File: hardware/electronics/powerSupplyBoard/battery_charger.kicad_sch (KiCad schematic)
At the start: 35 parts, among them J5 VAL, J6 VAL, Q1 BUK961R6, U1 BQ25798

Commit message: renamed bms board to power supply board
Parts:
- D1: footprint (none) -> DS-LED-SMD:LTST-1206
- F1: footprint (none) -> DS-Fuses:PTS1206
- L1: footprint (none) -> DS-Inductors-SMD:HCM1A1105V2
- Q1: footprint (none) -> DS-Package-SO:SOT404
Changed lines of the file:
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@@
 		)
 		(instances
-			(project "bms_breakout"
+			(project "powerSupplyBoard"
 				(path "/6f3ae1d2-e925-4178-b812-ea14ec542b6c/391a8be7-2326-4149-9988-5c06224e0655"
 					(reference "C4")
@@
 		)
 		(instances
-			(project "bms_breakout"
+			(project "powerSupplyBoard"
 				(path "/6f3ae1d2-e925-4178-b812-ea14ec542b6c/391a8be7-2326-4149-9988-5c06224e0655"
 					(reference "#PWR016")
@@
 		)
 		(instances
-			(project "bms_breakout"
+			(project "powerSupplyBoard"
 				(path "/6f3ae1d2-e925-4178-b812-ea14ec542b6c/391a8be7-2326-4149-9988-5c06224e0655"
 					(reference "C3")
@@
 			)
 		)
-		(property "Footprint" ""
+		(property "Footprint" "DS-Fuses:PTS1206"
 			(at 67.31 78.74 90)
 			(effects
@@
 		)
 		(instances
-			(project "bms_breakout"
+			(project "powerSupplyBoard"
 				(path "/6f3ae1d2-e925-4178-b812-ea14ec542b6c/391a8be7-2326-4149-9988-5c06224e0655"
 					(reference "F1")
@@
 		)
 		(instances
-			(project "bms_breakout"
+			(project "powerSupplyBoard"
 				(path "/6f3ae1d2-e925-4178-b812-ea14ec542b6c/391a8be7-2326-4149-9988-5c06224e0655"
 					(reference "C18")
@@
 		)
 		(instances
-			(project "bms_breakout"
+			(project "powerSupplyBoard"
 				(path "/6f3ae1d2-e925-4178-b812-ea14ec542b6c/391a8be7-2326-4149-9988-5c06224e0655"
 					(reference "C8")
@@
 		)
 		(instances
-			(project "bms_breakout"
+			(project "powerSupplyBoard"
 				(path "/6f3ae1d2-e925-4178-b812-ea14ec542b6c/391a8be7-2326-4149-9988-5c06224e0655"
 					(reference "C14")
@@
 		)
 		(instances
-			(project "bms_breakout"
+			(project "powerSupplyBoard"
 				(path "/6f3ae1d2-e925-4178-b812-ea14ec542b6c/391a8be7-2326-4149-9988-5c06224e0655"
 					(reference "R8")
@@
 		)
 		(instances
-			(project "bms_breakout"
+			(project "powerSupplyBoard"
 				(path "/6f3ae1d2-e925-4178-b812-ea14ec542b6c/391a8be7-2326-4149-9988-5c06224e0655"
 					(reference "#+3V02")
@@
 		)
 		(instances
-			(project "bms_breakout"
+			(project "powerSupplyBoard"
 				(path "/6f3ae1d2-e925-4178-b812-ea14ec542b6c/391a8be7-2326-4149-9988-5c06224e0655"
 					(reference "C2")
@@
 		)
 		(instances
-			(project "bms_breakout"
+			(project "powerSupplyBoard"
 				(path "/6f3ae1d2-e925-4178-b812-ea14ec542b6c/391a8be7-2326-4149-9988-5c06224e0655"
 					(reference "#PWR01")
@@
 		)
 		(instances
-			(project "bms_breakout"
+			(project "powerSupplyBoard"
 				(path "/6f3ae1d2-e925-4178-b812-ea14ec542b6c/391a8be7-2326-4149-9988-5c06224e0655"
 					(reference "R1")
@@
 		)
 		(instances
-			(project "bms_breakout"
+			(project "powerSupplyBoard"
 				(path "/6f3ae1d2-e925-4178-b812-ea14ec542b6c/391a8be7-2326-4149-9988-5c06224e0655"
 					(reference "#PWR017")
@@
 		)
 		(instances
-			(project "bms_breakout"
+			(project "powerSupplyBoard"
 				(path "/6f3ae1d2-e925-4178-b812-ea14ec542b6c/391a8be7-2326-4149-9988-5c06224e0655"
 					(reference "C11")
@@
 		)
 		(instances
-			(project "bms_breakout"
+			(project "powerSupplyBoard"
 				(path "/6f3ae1d2-e925-4178-b812-ea14ec542b6c/391a8be7-2326-4149-9988-5c06224e0655"
 					(reference "#PWR011")
@@
 		)
 		(instances
-			(project "bms_breakout"
+			(project "powerSupplyBoard"
 				(path "/6f3ae1d2-e925-4178-b812-ea14ec542b6c/391a8be7-2326-4149-9988-5c06224e0655"
 					(reference "C7")
@@
 		)
 		(instances
-			(project "bms_breakout"
+			(project "powerSupplyBoard"
 				(path "/6f3ae1d2-e925-4178-b812-ea14ec542b6c/391a8be7-2326-4149-9988-5c06224e0655"
 					(reference "#PWR03")
@@
 		)
 		(instances
-			(project "bms_breakout"
+			(project "powerSupplyBoard"
 				(path "/6f3ae1d2-e925-4178-b812-ea14ec542b6c/391a8be7-2326-4149-9988-5c06224e0655"
 					(reference "U1")
@@
 		)
 		(instances
-			(project "bms_breakout"
+			(project "powerSupplyBoard"
 				(path "/6f3ae1d2-e925-4178-b812-ea14ec542b6c/391a8be7-2326-4149-9988-5c06224e0655"
 					(reference "#+3V01")
@@
 		)
 		(instances
-			(project "bms_breakout"
+			(project "powerSupplyBoard"
 				(path "/6f3ae1d2-e925-4178-b812-ea14ec542b6c/391a8be7-2326-4149-9988-5c06224e0655"
 					(reference "R6")
@@
 		)
 		(instances
-			(project "bms_breakout"
+			(project "powerSupplyBoard"
 				(path "/6f3ae1d2-e925-4178-b812-ea14ec542b6c/391a8be7-2326-4149-9988-5c06224e0655"
 					(reference "C16")
@@
 		)
 		(instances
-			(project "bms_breakout"
+			(project "powerSupplyBoard"
 				(path "/6f3ae1d2-e925-4178-b812-ea14ec542b6c/391a8be7-2326-4149-9988-5c06224e0655"
 					(reference "#VIN01")
@@
 		)
 		(instances
-			(project "bms_breakout"
+			(project "powerSupplyBoard"
 				(path "/6f3ae1d2-e925-4178-b812-ea14ec542b6c/391a8be7-2326-4149-9988-5c06224e0655"
 					(reference "TH1")
@@
 		)
 		(instances
-			(project "bms_breakout"
+			(project "powerSupplyBoard"
 				(path "/6f3ae1d2-e925-4178-b812-ea14ec542b6c/391a8be7-2326-4149-9988-5c06224e0655"
 					(reference "R4")
@@
 		)
 		(instances
-			(project "bms_breakout"
+			(project "powerSupplyBoard"
 				(path "/6f3ae1d2-e925-4178-b812-ea14ec542b6c/391a8be7-2326-4149-9988-5c06224e0655"
 					(reference "C5")
@@
 		)
 		(instances
-			(project "bms_breakout"
+			(project "powerSupplyBoard"
 				(path "/6f3ae1d2-e925-4178-b812-ea14ec542b6c/391a8be7-2326-4149-9988-5c06224e0655"
 					(reference "#PWR012")
@@
 		)
 		(instances
-			(project "bms_breakout"
+			(project "powerSupplyBoard"
 				(path "/6f3ae1d2-e925-4178-b812-ea14ec542b6c/391a8be7-2326-4149-9988-5c06224e0655"
 					(reference "#PWR031")
@@
 			)
 		)
-		(property "Footprint" ""
+		(property "Footprint" "DS-Package-SO:SOT404"
 			(at 151.13 109.855 90)
 			(effects
@@
 		)
 		(instances
-			(project "bms_breakout"
+			(project "powerSupplyBoard"
 				(path "/6f3ae1d2-e925-4178-b812-ea14ec542b6c/391a8be7-2326-4149-9988-5c06224e0655"
 					(reference "R3")
@@
 		)
 		(instances
-			(project "bms_breakout"
+			(project "powerSupplyBoard"
 				(path "/6f3ae1d2-e925-4178-b812-ea14ec542b6c/391a8be7-2326-4149-9988-5c06224e0655"
 					(reference "#PWR015")
@@
 		)
 		(instances
-			(project "bms_breakout"
+			(project "powerSupplyBoard"
 				(path "/6f3ae1d2-e925-4178-b812-ea14ec542b6c/391a8be7-2326-4149-9988-5c06224e0655"
 					(reference "#PWR032")
@@
 		)
 		(instances
-			(project "bms_breakout"
+			(project "powerSupplyBoard"
 				(path "/6f3ae1d2-e925-4178-b812-ea14ec542b6c/391a8be7-2326-4149-9988-5c06224e0655"
 					(reference "C19")
@@
 		)
 		(instances
-			(project "bms_breakout"
+			(project "powerSupplyBoard"
 				(path "/6f3ae1d2-e925-4178-b812-ea14ec542b6c/391a8be7-2326-4149-9988-5c06224e0655"
 					(reference "C6")
@@
 		)
 		(instances
-			(project "bms_breakout"
+			(project "powerSupplyBoard"
 				(path "/6f3ae1d2-e925-4178-b812-ea14ec542b6c/391a8be7-2326-4149-9988-5c06224e0655"
 					(reference "C12")
@@
 		)
 		(instances
-			(project "bms_breakout"
+			(project "powerSupplyBoard"
 				(path "/6f3ae1d2-e925-4178-b812-ea14ec542b6c/391a8be7-2326-4149-9988-5c06224e0655"
 					(reference "C9")
@@
 			)
 		)
-		(property "Footprint" ""
+		(property "Footprint" "DS-Inductors-SMD:HCM1A1105V2"
 			(at 85.09 113.03 90)
 			(effects
@@
 		)
 		(instances
-			(project "bms_breakout"
+			(project "powerSupplyBoard"
 				(path "/6f3ae1d2-e925-4178-b812-ea14ec542b6c/391a8be7-2326-4149-9988-5c06224e0655"
 					(reference "#PWR014")
@@
 		)
 		(instances
-			(project "bms_breakout"
+			(project "powerSupplyBoard"
 				(path "/6f3ae1d2-e925-4178-b812-ea14ec542b6c/391a8be7-2326-4149-9988-5c06224e0655"
 					(reference "C13")
@@
 		)
 		(instances
-			(project "bms_breakout"
+			(project "powerSupplyBoard"
 				(path "/6f3ae1d2-e925-4178-b812-ea14ec542b6c/391a8be7-2326-4149-9988-5c06224e0655"
 					(reference "#PWR013")
@@
 		)
 		(instances
-			(project "bms_breakout"
+			(project "powerSupplyBoard"
 				(path "/6f3ae1d2-e925-4178-b812-ea14ec542b6c/391a8be7-2326-4149-9988-5c06224e0655"
 					(reference "C17")
@@
 		)
 		(instances
-			(project "bms_breakout"
+			(project "powerSupplyBoard"
 				(path "/6f3ae1d2-e925-4178-b812-ea14ec542b6c/391a8be7-2326-4149-9988-5c06224e0655"
 					(reference "R2")
@@
 		)
 		(instances
-			(project "bms_breakout"
+			(project "powerSupplyBoard"
 				(path "/6f3ae1d2-e925-4178-b812-ea14ec542b6c/391a8be7-2326-4149-9988-5c06224e0655"
 					(reference "R5")
@@
 		)
 		(instances
-			(project "bms_breakout"
+			(project "powerSupplyBoard"
 				(path "/6f3ae1d2-e925-4178-b812-ea14ec542b6c/391a8be7-2326-4149-9988-5c06224e0655"
 					(reference "C10")
@@
 		)
 		(instances
-			(project "bms_breakout"
+			(project "powerSupplyBoard"
 				(path "/6f3ae1d2-e925-4178-b812-ea14ec542b6c/391a8be7-2326-4149-9988-5c06224e0655"
 					(reference "C1")
@@
 		)
 		(instances
-			(project "bms_breakout"
+			(project "powerSupplyBoard"
 				(path "/6f3ae1d2-e925-4178-b812-ea14ec542b6c/391a8be7-2326-4149-9988-5c06224e0655"
 					(reference "R7")
@@
 		)
 		(instances
-			(project "bms_breakout"
+			(project "powerSupplyBoard"
 				(path "/6f3ae1d2-e925-4178-b812-ea14ec542b6c/391a8be7-2326-4149-9988-5c06224e0655"
 					(reference "C15")
@@
 			)
 		)
-		(property "Footprint" ""
+		(property "Footprint" "DS-LED-SMD:LTST-1206"
 			(at 93.98 130.81 0)
 			(effects

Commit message: added footprint for BQ25798
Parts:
- U1: footprint (none) -> DS-PMIC-SMD:RQM0029A
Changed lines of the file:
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@@
 			)
 		)
-		(property "Footprint" ""
+		(property "Footprint" "DS-PMIC-SMD:RQM0029A"
 			(at 114.3 110.49 0)
 			(effects

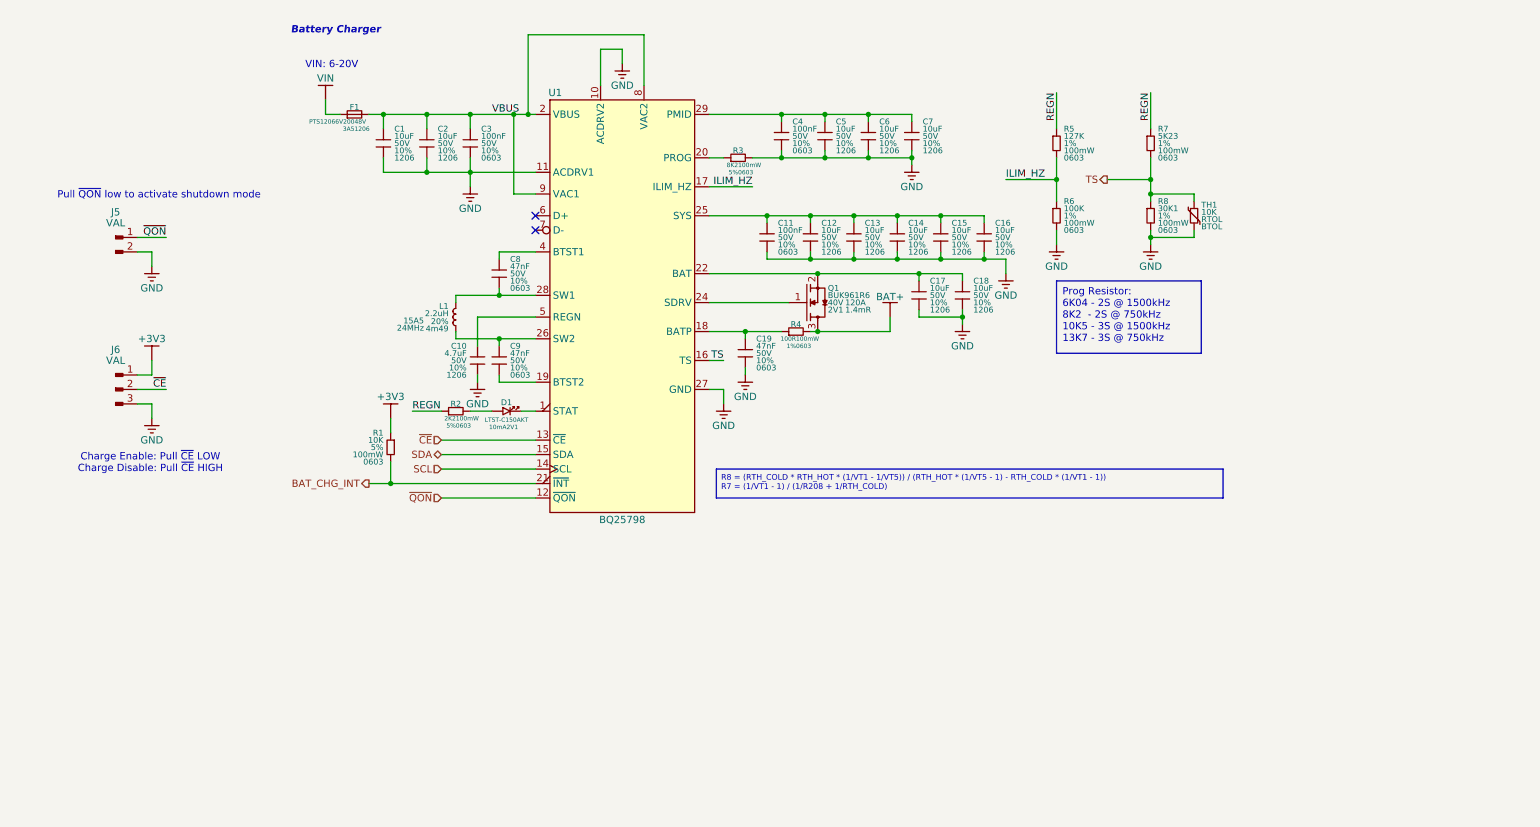
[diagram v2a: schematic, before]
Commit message: renumbers passives and cleaned up sheets
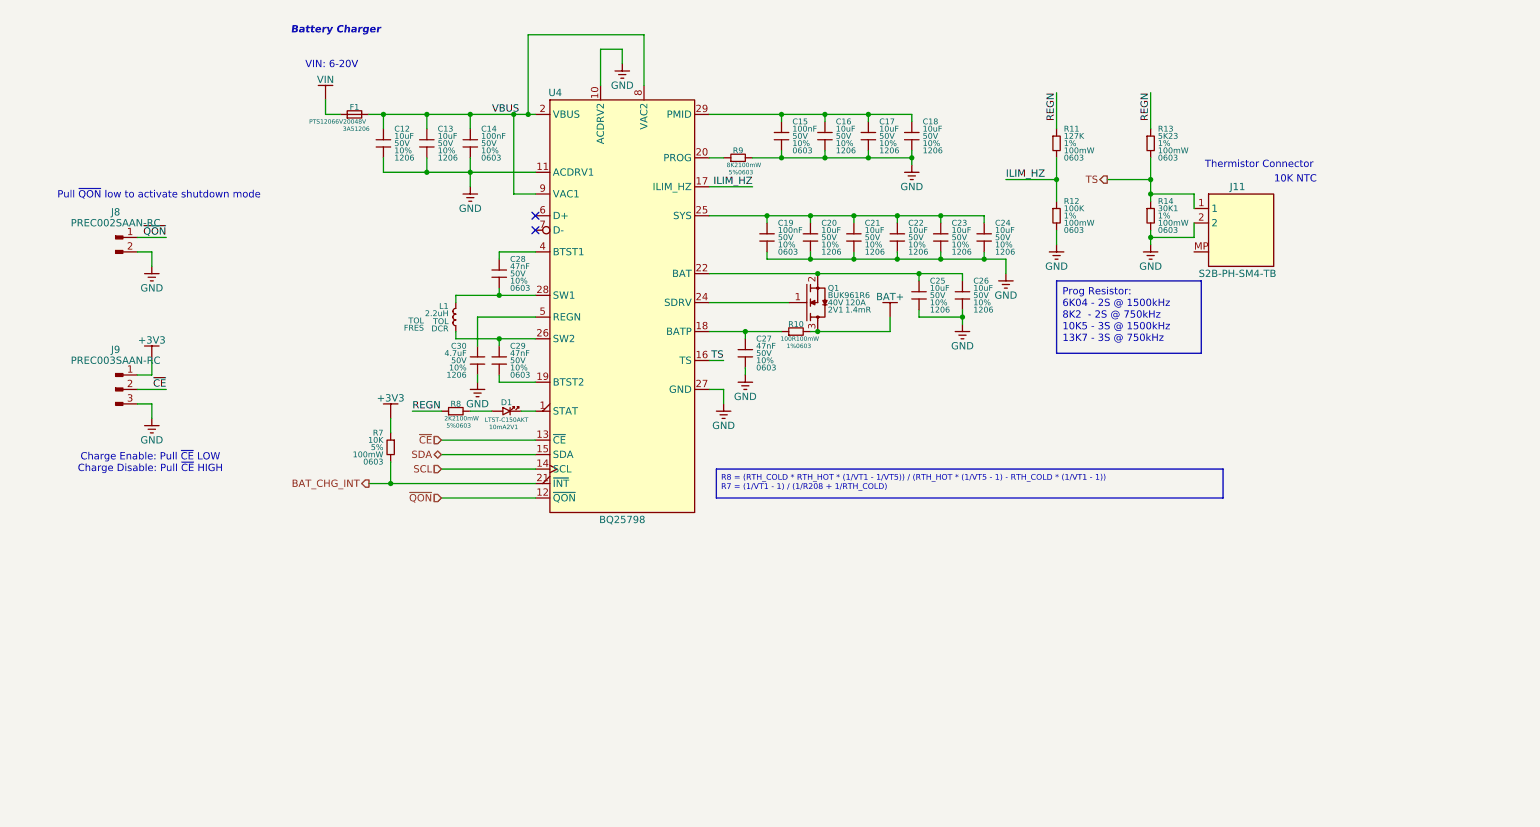
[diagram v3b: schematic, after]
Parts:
- removed TH1: 10K, symbol DSE-Passives:Thermistor
- added J11: S2B-PH-SM4-TB, DS-Rectangular-Connectors:JST-PH-S2B-SM4-TB, symbol DS-Connectors:S2B-PH-SM4-TB
- C12: renamed from C1; symbol DS-Passives:C -> lib_sch:C_2
- C13: renamed from C2; symbol DS-Passives:C -> lib_sch:C_2
- C14: renamed from C3; symbol DS-Passives:C -> lib_sch:C_2
- C15: renamed from C4; symbol DS-Passives:C -> lib_sch:C_2
- C16: renamed from C5; symbol DS-Passives:C -> lib_sch:C_2
- C17: renamed from C6; symbol DS-Passives:C -> lib_sch:C_2
- C18: renamed from C7; symbol DS-Passives:C -> lib_sch:C_2
- C19: renamed from C11; symbol DS-Passives:C -> lib_sch:C_2
- C20: renamed from C12; symbol DS-Passives:C -> lib_sch:C_2
- C21: renamed from C13; symbol DS-Passives:C -> lib_sch:C_2
- C22: renamed from C14; symbol DS-Passives:C -> lib_sch:C_2
- C23: renamed from C15; symbol DS-Passives:C -> lib_sch:C_2
- C24: renamed from C16; symbol DS-Passives:C -> lib_sch:C_2
- C25: renamed from C17; symbol DS-Passives:C -> lib_sch:C_2
- C26: renamed from C18; symbol DS-Passives:C -> lib_sch:C_2
- C27: renamed from C19; symbol DS-Passives:C -> lib_sch:C_2
- C28: renamed from C8; symbol DS-Passives:C -> lib_sch:C_2
- C29: renamed from C9; symbol DS-Passives:C -> lib_sch:C_2
- C30: renamed from C10; footprint 12065C475K4T4A -> DS-Capacitors-SMD:MLCC1206; symbol DS-Passives:C -> lib_sch:C_2
- D1: symbol DS-LEDs:LED_horizontal -> lib_sch:LED_horizontal
- F1: symbol DS-Passives:F_horizontal -> lib_sch:F_horizontal
- J8: renamed from J5; value VAL -> PREC002SAAN-RC; footprint (none) -> DS-Rectangular-Connectors:conn_01x02_254; symbol DS-Connectors:Conn_01x02_Pin -> lib_sch:Conn_01x02_Pin; DKPN (none) -> S1012EC-02-ND; MPN (none) -> PREC002SAAN-RC; Manufacturer (none) -> Sullins Connector Solutions
- J9: renamed from J6; value VAL -> PREC003SAAN-RC; footprint (none) -> DS-Rectangular-Connectors:conn_01x03_254; symbol DS-Connectors:Conn_01x03_Pin -> lib_sch:Conn_01x03_Pin; DKPN (none) -> S1012EC-03-ND; MPN (none) -> PREC003SAAN-RC; Manufacturer (none) -> Sullins Connector Solutions
- L1: symbol DS-Passives:L -> lib_sch:L; Current Rating 15A5 -> TOL; DC Resistance 4m49 -> DCR; Resonant Frequency 24MHz -> FRES; Tolerance 20% -> TOL
- Q1: symbol DS-Transistors:NMOS_GSD -> lib_sch:NMOS_GSD_1
- R10: renamed from R4; symbol DS-Passives:R_horizontal -> lib_sch:R_horizontal
- R11: renamed from R5; symbol DS-Passives:R -> lib_sch:R
- R12: renamed from R6; symbol DS-Passives:R -> lib_sch:R
- R13: renamed from R7; symbol DS-Passives:R -> lib_sch:R
- R14: renamed from R8; symbol DS-Passives:R -> lib_sch:R
- R7: renamed from R1; symbol DS-Passives:R -> lib_sch:R
- R8: renamed from R2; symbol DS-Passives:R_horizontal -> lib_sch:R_horizontal
- R9: renamed from R3; symbol DS-Passives:R_horizontal -> lib_sch:R_horizontal
- U4: renamed from U1; symbol DS-PMIC:BQ25798 -> lib_sch:BQ25798
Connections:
- net GND: now also J11.2
- net TS: now also J11.1
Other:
- note added: "10K NTC"
- note added: "Thermistor Connector"

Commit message: fixed schematic, organized page, and fixed ground nets
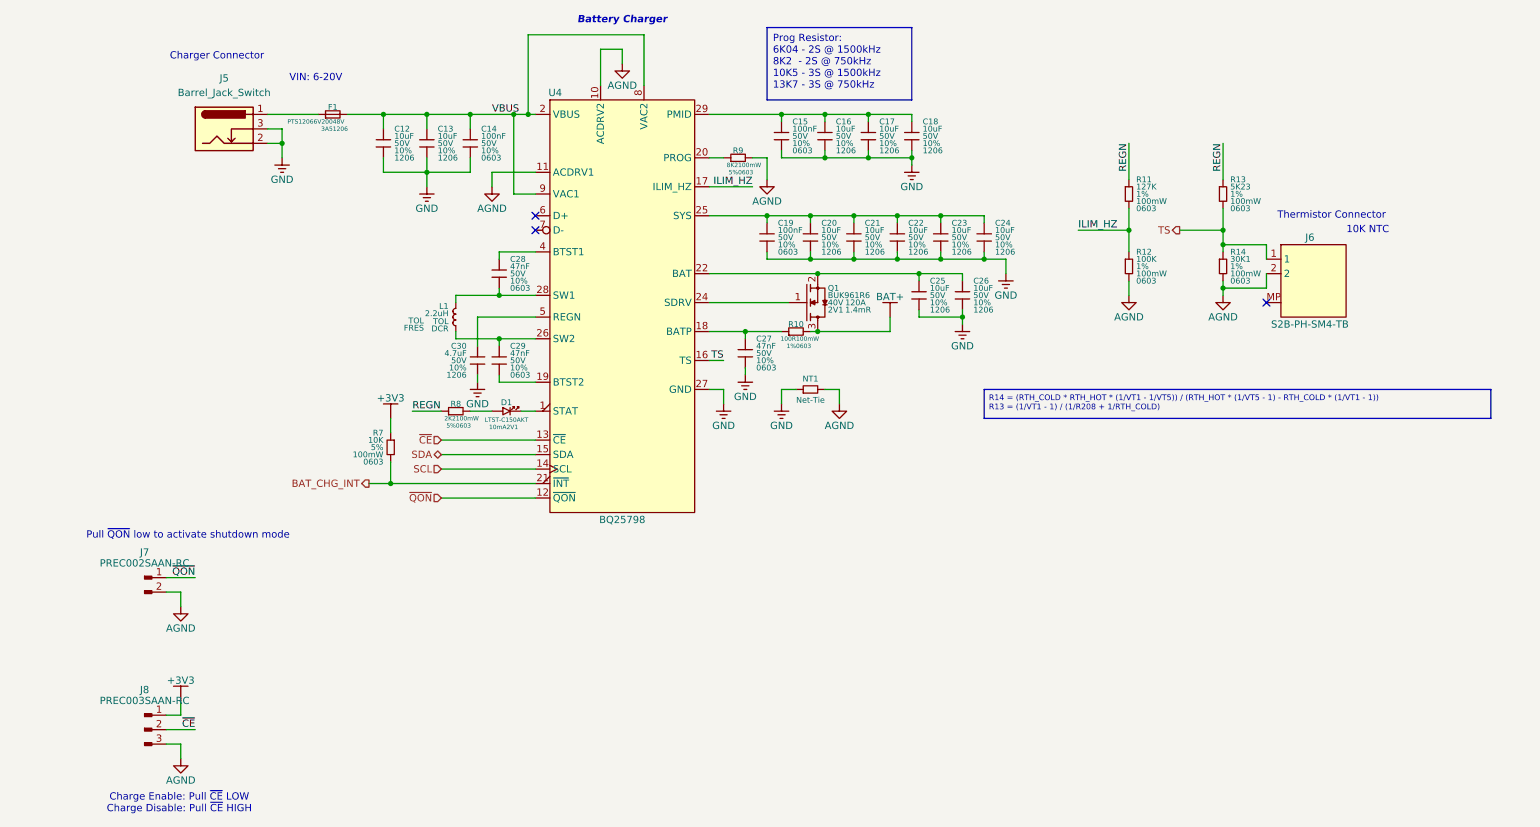
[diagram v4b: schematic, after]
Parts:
- added J5: Barrel_Jack_Switch, DS-Battery-Connectors:PJ-002A, symbol lib_sch:Barrel_Jack_Switch
- added NT1: Net-Tie, DS-Resistors-SMD:CRCW1210, symbol lib_sch:NT
- J6: renamed from J11; symbol DS-Connectors:S2B-PH-SM4-TB -> lib_sch:S2B-PH-SM4-TB
- renumbered J8 to J7, J9 to J8
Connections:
- net GND: now also J5.2, J5.3, NT1.1; no longer J6.2, J7.2, J8.3, R12.2, R14.2, R9.2, U4.10 (ACDRV2), U4.11 (ACDRV1)
- net VIN: no longer names the net of F1.1
- net VIN: now also J5.1
- new net AGND: J6.2, J7.2, J8.3, NT1.2, R12.2, R14.2, R9.2, U4.10 (ACDRV2), U4.11 (ACDRV1)
- no-connect marks 2 -> 3
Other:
- note added: "Charger Connector"
- moved on the sheet: F1, J6, J7, J8, R11, R12, R13, R14
